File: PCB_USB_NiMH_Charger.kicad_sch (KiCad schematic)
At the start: 65 parts, among them J1 USB_C_Receptacle_Simple, J2 Conn_02x01, J5 Conn_02x01, J6 Conn_02x01, Q1 2SA1015, Q2 2SC1815, Q3 2SB834, Q4 2SC1815, Q5 2SB834, Q6 2SC1815, Q7 2SB834, Q8 2SC1815, Q9 2SB834, U1 LM339, U2 S-812C33A_TO92

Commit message: Update
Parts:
- removed J5, J6: Conn_02x01, Connector_PinHeader_2.54mm:PinHeader_1x02_P2.54mm_Vertical, symbol Connector_Generic:Conn_02x01
- removed R18, R24: 15, Resistor_THT:R_Axial_DIN0207_L6.3mm_D2.5mm_P2.54mm_Vertical, symbol Device:R
- BT1, BT2: value Battery_Cell -> Battery_Cell (AAA)
- BT3, BT4: value Battery_Cell -> Battery_Cell (AA)
- C2, C3: footprint Capacitor_THT:CP_Radial_D5.0mm_P2.50mm -> Capacitor_THT:CP_Radial_D5.0mm_P2.00mm
- J1: footprint mylib:Connector_USB_C_simple -> mylib:USB_C_Receptacle_CUI_Devices_UJC-HP-3-SMT-TR; symbol mylib:USB_C_Receptacle_Simple -> Connector:USB_C_Receptacle_PowerOnly_6P
- Q2, Q4, Q6, Q8: value 2SC1815 -> 2SC2458; footprint Package_TO_SOT_THT:TO-92_Inline_Wide -> Package_TO_SOT_THT:TO-92S_Wide; symbol Transistor_BJT:2SC1815 -> mylib:2SC2458
- R1, R2: footprint Resistor_THT:R_Axial_DIN0204_L3.6mm_D1.6mm_P5.08mm_Horizontal -> Resistor_THT:R_Axial_DIN0204_L3.6mm_D1.6mm_P2.54mm_Vertical
- R19, R25: value 10 -> 5.6
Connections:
- net +5V: now also R19.1, R25.1
- net GND: no longer J1.4 (GND), J1.7 (GND)
- net Vref: no longer C7.2, U1.11 (+)
- net VBUS: now reaches F1.2, J1.A9 (VBUS), J1.B9 (VBUS)
- net VBUS: no longer J1.1 (VBUS), J1.B4 (VBUS)
- net at R1.2: now also J1.A5 (CC1); no longer J1.5 (CC1)
- net at R2.2: now also J1.B5 (CC2); no longer J1.6 (CC2)
- new net: C7.2, U1.11 (+)
- no-connect marks 3 -> 1
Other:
- moved on the sheet: BT2, BT3, C6, C7, D3, D4, Q4, Q5, Q6, Q7, R1, R11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

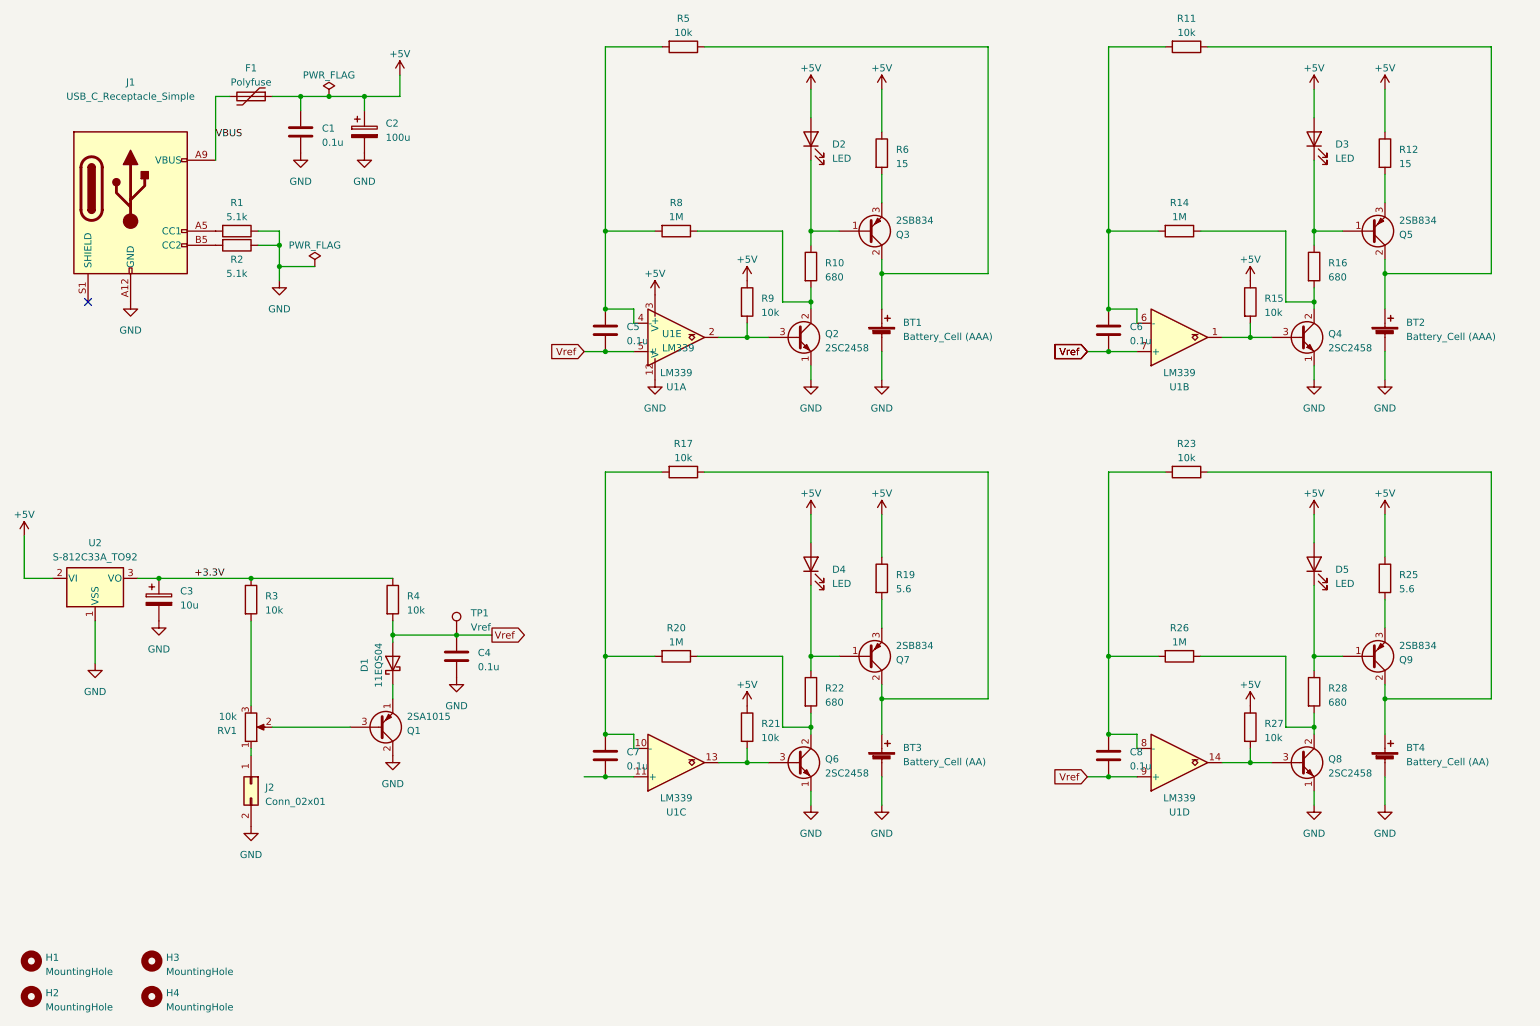
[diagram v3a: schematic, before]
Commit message: Update to rev. 3
* LED を低消費電力版に変更し、LM339 で直接駆動するように変更。
  - 2SC1815 (2SC2458) を削除。
  - プルアップ抵抗を削除。
  - 680Ω を 2KΩ に変更。
* 10μF 電解コンデンサーを積層セラミックコンデンサーに変更。
* 2SB834 を裏面に配置。
* USB コネクタのフットプリントに間違いがあったのを修正。
  (取り付け穴が空いていなかったのを修正。)
* 配線を完了。
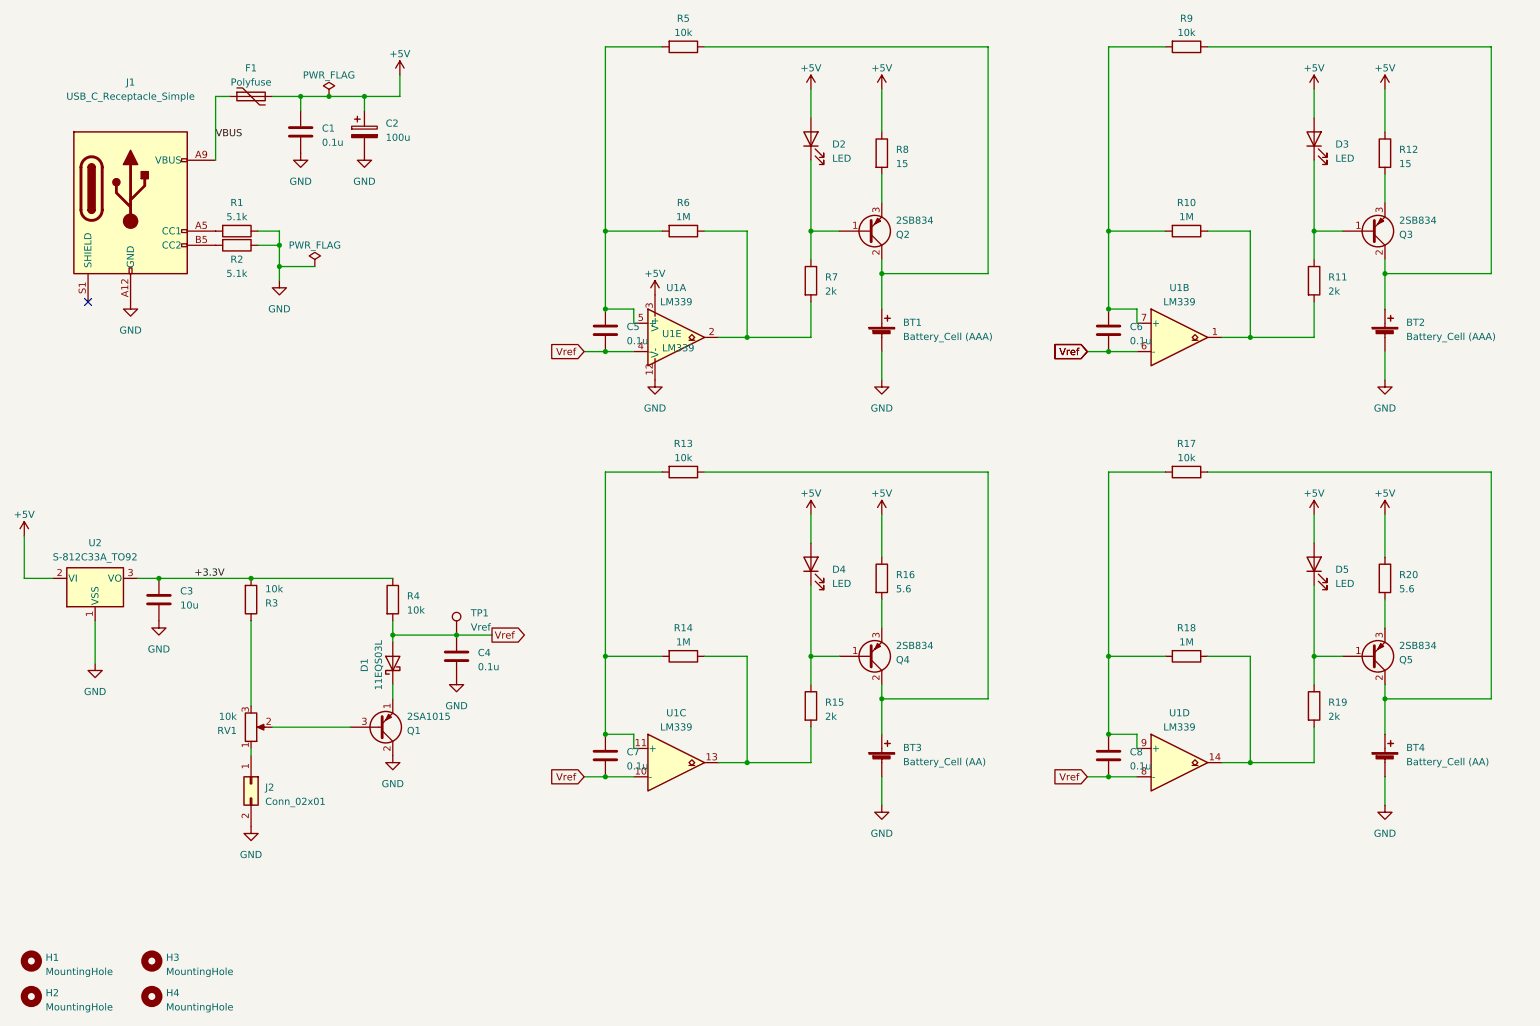
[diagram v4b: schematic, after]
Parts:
- removed Q2, Q4, Q6, Q8: 2SC2458, Package_TO_SOT_THT:TO-92S_Wide, symbol mylib:2SC2458
- removed R15, R21, R27, R9: 10k, Resistor_THT:R_Axial_DIN0207_L6.3mm_D2.5mm_P2.54mm_Vertical, symbol Device:R
- C3: footprint Capacitor_THT:CP_Radial_D5.0mm_P2.00mm -> Capacitor_THT:C_Disc_D4.7mm_W2.5mm_P5.00mm; symbol Device:C_Polarized -> Device:C
- D1: value 11EQS04 -> 11EQS03L
- Q2: renamed from Q3; footprint Package_TO_SOT_THT:TO-220-3_Vertical -> Package_TO_SOT_THT:TO-220-3_Horizontal_TabDown
- Q3: renamed from Q5; footprint Package_TO_SOT_THT:TO-220-3_Vertical -> Package_TO_SOT_THT:TO-220-3_Horizontal_TabDown
- Q4: renamed from Q7; footprint Package_TO_SOT_THT:TO-220-3_Vertical -> Package_TO_SOT_THT:TO-220-3_Horizontal_TabDown
- Q5: renamed from Q9; footprint Package_TO_SOT_THT:TO-220-3_Vertical -> Package_TO_SOT_THT:TO-220-3_Horizontal_TabDown
- R1, R2: footprint Resistor_THT:R_Axial_DIN0204_L3.6mm_D1.6mm_P2.54mm_Vertical -> Resistor_THT:R_Axial_DIN0204_L3.6mm_D1.6mm_P5.08mm_Horizontal
- R11: renamed from R16; value 680 -> 2k
- R12, R3: footprint Resistor_THT:R_Axial_DIN0207_L6.3mm_D2.5mm_P2.54mm_Vertical -> Resistor_THT:R_Axial_DIN0207_L6.3mm_D2.5mm_P7.62mm_Horizontal
- R15: renamed from R22; value 680 -> 2k
- R16: renamed from R19; footprint Resistor_THT:R_Axial_DIN0207_L6.3mm_D2.5mm_P2.54mm_Vertical -> Resistor_THT:R_Axial_DIN0207_L6.3mm_D2.5mm_P7.62mm_Horizontal
- R19: renamed from R28; value 680 -> 2k
- R20: renamed from R25; footprint Resistor_THT:R_Axial_DIN0207_L6.3mm_D2.5mm_P2.54mm_Vertical -> Resistor_THT:R_Axial_DIN0207_L6.3mm_D2.5mm_P7.62mm_Horizontal
- R7: renamed from R10; value 680 -> 2k
- R8: renamed from R6; footprint Resistor_THT:R_Axial_DIN0207_L6.3mm_D2.5mm_P2.54mm_Vertical -> Resistor_THT:R_Axial_DIN0207_L6.3mm_D2.5mm_P7.62mm_Horizontal
- renumbered R14 to R10, R17 to R13, R20 to R14, R23 to R17, R26 to R18, R8 to R6, R11 to R9
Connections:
- net +3.3V: now also R3.2; no longer R3.1
- net +5V: now also F1.2; no longer F1.1
- net VBUS: now also F1.1; no longer F1.2
- net Vref: now also C7.2, U1.10 (-), U1.4 (-), U1.6 (-), U1.8 (-); no longer U1.5 (+), U1.7 (+), U1.9 (+)
- net at R10.1, R11.2: now also U1.1
- net at U1.2: now also R6.1, R7.2
- net at C5.1, R5.2, R6.2: now also U1.5 (+); no longer U1.4 (-)
- net at R18.1, R19.2: now also U1.14
- net at C8.1, R17.2, R18.2: now also U1.9 (+); no longer U1.8 (-)
- net at C6.1, R10.2, R9.2: now also U1.7 (+); no longer U1.6 (-)
- net at RV1.3: now also R3.1; no longer R3.2
- net at R14.1, R15.2: now also U1.13
- net at C7.1, R13.2, R14.2: now also U1.11 (+); no longer U1.10 (-)
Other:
- moved on the sheet: F1, R10, R11, R14, R15, R18, R19, R6, R7
